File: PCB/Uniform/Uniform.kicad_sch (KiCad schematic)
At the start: 156 parts, among them CON1 826629-5, CON2 Conn_01x03, U1 STM32L072KZT6

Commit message: about to attempt rotating the MCU
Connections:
- net C0: now also U1.6 (PA0); no longer U1.11 (PA5)
- net C1: now also U1.7 (PA1); no longer U1.12 (PA6)
- net C10: now also U1.18 (PA8); no longer U1.27 (PB4)
- net C11: now also U1.19 (PA9); no longer U1.28 (PB5)
- net C12: now also U1.20 (PA10); no longer U1.29 (PB6)
- net C13: now also U1.25 (PA15); no longer U1.30 (PB7)
- net C2: now also U1.8 (PA2); no longer U1.13 (PA7)
- net C3: now also U1.9 (PA3); no longer U1.14 (PB0)
- net C4: now also U1.10 (PA4); no longer U1.15 (PB1)
- net C5: now also U1.11 (PA5); no longer U1.18 (PA8)
- net C6: now also U1.12 (PA6); no longer U1.19 (PA9)
- net C7: now also U1.13 (PA7); no longer U1.20 (PA10)
- net C8: now also U1.14 (PB0); no longer U1.25 (PA15)
- net C9: now also U1.15 (PB1); no longer U1.26 (PB3)
- net R0: now also U1.30 (PB7); no longer U1.6 (PA0)
- net R1: now also U1.29 (PB6); no longer U1.7 (PA1)
- net R2: now also U1.28 (PB5); no longer U1.8 (PA2)
- net R3: now also U1.27 (PB4); no longer U1.9 (PA3)
- net R4: now also U1.26 (PB3); no longer U1.10 (PA4)
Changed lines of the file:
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@@
     )
   )
-  (global_label "C0" (shape input) (at 349.25 92.71 270) (fields_autoplaced)
-    (effects (font (size 1.27 1.27)) (justify right))
-    (property "Intersheet References" "${INTERSHEET_REFS}" (id 0) (at 0 0 0)
-      (effects (font (size 1.27 1.27)) hide)
-    )
-  )
-  (global_label "C9" (shape input) (at 359.41 34.29 90) (fields_autoplaced)
-    (effects (font (size 1.27 1.27)) (justify left))
-    (property "Intersheet References" "${INTERSHEET_REFS}" (id 0) (at 0 0 0)
+  (global_label "C0" (shape input) (at 323.85 67.31 180) (fields_autoplaced)
+    (effects (font (size 1.27 1.27)) (justify right))
+    (property "Intersheet References" "${INTERSHEET_REFS}" (id 0) (at 416.56 -281.94 0)
+      (effects (font (size 1.27 1.27)) hide)
+    )
+  )
+  (global_label "C9" (shape input) (at 359.41 92.71 270) (fields_autoplaced)
+    (effects (font (size 1.27 1.27)) (justify right))
+    (property "Intersheet References" "${INTERSHEET_REFS}" (id 0) (at 718.82 127 0)
       (effects (font (size 1.27 1.27)) hide)
     )
@@
     )
   )
-  (global_label "R1" (shape input) (at 323.85 69.85 180) (fields_autoplaced)
-    (effects (font (size 1.27 1.27)) (justify right))
-    (property "Intersheet References" "${INTERSHEET_REFS}" (id 0) (at 0 0 0)
+  (global_label "R1" (shape input) (at 351.79 34.29 90) (fields_autoplaced)
+    (effects (font (size 1.27 1.27)) (justify left))
+    (property "Intersheet References" "${INTERSHEET_REFS}" (id 0) (at 421.64 -289.56 0)
       (effects (font (size 1.27 1.27)) hide)
     )
@@
     )
   )
-  (global_label "R2" (shape input) (at 323.85 72.39 180) (fields_autoplaced)
-    (effects (font (size 1.27 1.27)) (justify right))
-    (property "Intersheet References" "${INTERSHEET_REFS}" (id 0) (at 0 0 0)
-      (effects (font (size 1.27 1.27)) hide)
-    )
-  )
-  (global_label "C7" (shape input) (at 382.27 64.77 0) (fields_autoplaced)
-    (effects (font (size 1.27 1.27)) (justify left))
-    (property "Intersheet References" "${INTERSHEET_REFS}" (id 0) (at 0 0 0)
+  (global_label "R2" (shape input) (at 354.33 34.29 90) (fields_autoplaced)
+    (effects (font (size 1.27 1.27)) (justify left))
+    (property "Intersheet References" "${INTERSHEET_REFS}" (id 0) (at 426.72 -289.56 0)
+      (effects (font (size 1.27 1.27)) hide)
+    )
+  )
+  (global_label "C7" (shape input) (at 354.33 92.71 270) (fields_autoplaced)
+    (effects (font (size 1.27 1.27)) (justify right))
+    (property "Intersheet References" "${INTERSHEET_REFS}" (id 0) (at 419.1 -289.56 0)
       (effects (font (size 1.27 1.27)) hide)
     )
@@
     )
   )
-  (global_label "R0" (shape input) (at 323.85 67.31 180) (fields_autoplaced)
-    (effects (font (size 1.27 1.27)) (justify right))
-    (property "Intersheet References" "${INTERSHEET_REFS}" (id 0) (at 0 0 0)
-      (effects (font (size 1.27 1.27)) hide)
-    )
-  )
-  (global_label "C3" (shape input) (at 356.87 92.71 270) (fields_autoplaced)
-    (effects (font (size 1.27 1.27)) (justify right))
-    (property "Intersheet References" "${INTERSHEET_REFS}" (id 0) (at 0 0 0)
+  (global_label "R0" (shape input) (at 349.25 34.29 90) (fields_autoplaced)
+    (effects (font (size 1.27 1.27)) (justify left))
+    (property "Intersheet References" "${INTERSHEET_REFS}" (id 0) (at 416.56 -289.56 0)
+      (effects (font (size 1.27 1.27)) hide)
+    )
+  )
+  (global_label "C3" (shape input) (at 344.17 92.71 270) (fields_autoplaced)
+    (effects (font (size 1.27 1.27)) (justify right))
+    (property "Intersheet References" "${INTERSHEET_REFS}" (id 0) (at -12.7 0 0)
       (effects (font (size 1.27 1.27)) hide)
     )
@@
     )
   )
-  (global_label "C5" (shape input) (at 382.27 69.85 0) (fields_autoplaced)
-    (effects (font (size 1.27 1.27)) (justify left))
-    (property "Intersheet References" "${INTERSHEET_REFS}" (id 0) (at 0 0 0)
+  (global_label "C5" (shape input) (at 349.25 92.71 270) (fields_autoplaced)
+    (effects (font (size 1.27 1.27)) (justify right))
+    (property "Intersheet References" "${INTERSHEET_REFS}" (id 0) (at 419.1 -289.56 0)
       (effects (font (size 1.27 1.27)) hide)
     )
@@
     )
   )
-  (global_label "R3" (shape input) (at 344.17 92.71 270) (fields_autoplaced)
-    (effects (font (size 1.27 1.27)) (justify right))
-    (property "Intersheet References" "${INTERSHEET_REFS}" (id 0) (at 0 0 0)
-      (effects (font (size 1.27 1.27)) hide)
-    )
-  )
-  (global_label "C4" (shape input) (at 359.41 92.71 270) (fields_autoplaced)
-    (effects (font (size 1.27 1.27)) (justify right))
-    (property "Intersheet References" "${INTERSHEET_REFS}" (id 0) (at 0 0 0)
+  (global_label "R3" (shape input) (at 356.87 34.29 90) (fields_autoplaced)
+    (effects (font (size 1.27 1.27)) (justify left))
+    (property "Intersheet References" "${INTERSHEET_REFS}" (id 0) (at 701.04 127 0)
+      (effects (font (size 1.27 1.27)) hide)
+    )
+  )
+  (global_label "C4" (shape input) (at 346.71 92.71 270) (fields_autoplaced)
+    (effects (font (size 1.27 1.27)) (justify right))
+    (property "Intersheet References" "${INTERSHEET_REFS}" (id 0) (at -12.7 0 0)
       (effects (font (size 1.27 1.27)) hide)
     )
@@
     )
   )
-  (global_label "R4" (shape input) (at 346.71 92.71 270) (fields_autoplaced)
-    (effects (font (size 1.27 1.27)) (justify right))
-    (property "Intersheet References" "${INTERSHEET_REFS}" (id 0) (at 0 0 0)
+  (global_label "R4" (shape input) (at 359.41 34.29 90) (fields_autoplaced)
+    (effects (font (size 1.27 1.27)) (justify left))
+    (property "Intersheet References" "${INTERSHEET_REFS}" (id 0) (at 706.12 127 0)
       (effects (font (size 1.27 1.27)) hide)
     )
@@
     )
   )
-  (global_label "C13" (shape input) (at 349.25 34.29 90) (fields_autoplaced)
-    (effects (font (size 1.27 1.27)) (justify left))
-    (property "Intersheet References" "${INTERSHEET_REFS}" (id 0) (at 0 0 0)
+  (global_label "C13" (shape input) (at 361.95 34.29 90) (fields_autoplaced)
+    (effects (font (size 1.27 1.27)) (justify left))
+    (property "Intersheet References" "${INTERSHEET_REFS}" (id 0) (at 12.7 0 0)
       (effects (font (size 1.27 1.27)) hide)
     )
@@
     )
   )
-  (global_label "C11" (shape input) (at 354.33 34.29 90) (fields_autoplaced)
-    (effects (font (size 1.27 1.27)) (justify left))
-    (property "Intersheet References" "${INTERSHEET_REFS}" (id 0) (at 0 0 0)
+  (global_label "C11" (shape input) (at 382.27 67.31 0) (fields_autoplaced)
+    (effects (font (size 1.27 1.27)) (justify left))
+    (property "Intersheet References" "${INTERSHEET_REFS}" (id 0) (at 416.56 -287.02 0)
       (effects (font (size 1.27 1.27)) hide)
     )
@@
     )
   )
-  (global_label "C8" (shape input) (at 361.95 34.29 90) (fields_autoplaced)
-    (effects (font (size 1.27 1.27)) (justify left))
-    (property "Intersheet References" "${INTERSHEET_REFS}" (id 0) (at 0 0 0)
-      (effects (font (size 1.27 1.27)) hide)
-    )
-  )
-  (global_label "C6" (shape input) (at 382.27 67.31 0) (fields_autoplaced)
-    (effects (font (size 1.27 1.27)) (justify left))
-    (property "Intersheet References" "${INTERSHEET_REFS}" (id 0) (at 0 0 0)
-      (effects (font (size 1.27 1.27)) hide)
-    )
-  )
-  (global_label "C2" (shape input) (at 354.33 92.71 270) (fields_autoplaced)
-    (effects (font (size 1.27 1.27)) (justify right))
-    (property "Intersheet References" "${INTERSHEET_REFS}" (id 0) (at 0 0 0)
+  (global_label "C8" (shape input) (at 356.87 92.71 270) (fields_autoplaced)
+    (effects (font (size 1.27 1.27)) (justify right))
+    (property "Intersheet References" "${INTERSHEET_REFS}" (id 0) (at 718.82 127 0)
+      (effects (font (size 1.27 1.27)) hide)
+    )
+  )
+  (global_label "C6" (shape input) (at 351.79 92.71 270) (fields_autoplaced)
+    (effects (font (size 1.27 1.27)) (justify right))
+    (property "Intersheet References" "${INTERSHEET_REFS}" (id 0) (at 419.1 -289.56 0)
+      (effects (font (size 1.27 1.27)) hide)
+    )
+  )
+  (global_label "C2" (shape input) (at 323.85 72.39 180) (fields_autoplaced)
+    (effects (font (size 1.27 1.27)) (justify right))
+    (property "Intersheet References" "${INTERSHEET_REFS}" (id 0) (at 416.56 -281.94 0)
       (effects (font (size 1.27 1.27)) hide)
     )
@@
     )
   )
-  (global_label "C1" (shape input) (at 351.79 92.71 270) (fields_autoplaced)
-    (effects (font (size 1.27 1.27)) (justify right))
-    (property "Intersheet References" "${INTERSHEET_REFS}" (id 0) (at 0 0 0)
-      (effects (font (size 1.27 1.27)) hide)
-    )
-  )
-  (global_label "C10" (shape input) (at 356.87 34.29 90) (fields_autoplaced)
-    (effects (font (size 1.27 1.27)) (justify left))
-    (property "Intersheet References" "${INTERSHEET_REFS}" (id 0) (at 0 0 0)
+  (global_label "C1" (shape input) (at 323.85 69.85 180) (fields_autoplaced)
+    (effects (font (size 1.27 1.27)) (justify right))
+    (property "Intersheet References" "${INTERSHEET_REFS}" (id 0) (at 416.56 -281.94 0)
+      (effects (font (size 1.27 1.27)) hide)
+    )
+  )
+  (global_label "C10" (shape input) (at 382.27 69.85 0) (fields_autoplaced)
+    (effects (font (size 1.27 1.27)) (justify left))
+    (property "Intersheet References" "${INTERSHEET_REFS}" (id 0) (at 416.56 -287.02 0)
       (effects (font (size 1.27 1.27)) hide)
     )
@@
     )
   )
-  (global_label "C12" (shape input) (at 351.79 34.29 90) (fields_autoplaced)
-    (effects (font (size 1.27 1.27)) (justify left))
-    (property "Intersheet References" "${INTERSHEET_REFS}" (id 0) (at 0 0 0)
-      (effects (font (size 1.27 1.27)) hide)
-    )
+  (global_label "C12" (shape input) (at 382.27 64.77 0) (fields_autoplaced)
+    (effects (font (size 1.27 1.27)) (justify left))
+    (property "Intersheet References" "${INTERSHEET_REFS}" (id 0) (at 416.56 -287.02 0)
+      (effects (font (size 1.27 1.27)) hide)
+    )

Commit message: PCB first pass complete
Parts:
- LED1: footprint LED_THT:LED_D5.0mm_Clear -> LED_THT:LED_D3.0mm_Clear
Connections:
- net C13: now also U1.29 (PB6); no longer U1.25 (PA15)
- net LED_DATA: now also U1.26 (PB3); no longer U1.2 (PC14-_OSC32_IN_(PC14))
- net R0: now also U1.27 (PB4); no longer U1.30 (PB7)
- net R1: now also U1.28 (PB5); no longer U1.29 (PB6)
- net R2: now also U1.30 (PB7); no longer U1.28 (PB5)
- net R3: now also U1.3 (PC15-_OSC32_OUT_(PC15)); no longer U1.27 (PB4)
- net R4: now also U1.2 (PC14-_OSC32_IN_(PC14)); no longer U1.26 (PB3)
- net STATUS_LED_DATA: now also U1.25 (PA15); no longer U1.3 (PC15-_OSC32_OUT_(PC15))
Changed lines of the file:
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@@
     )
   )
-  (global_label "R1" (shape input) (at 351.79 34.29 90) (fields_autoplaced)
+  (global_label "R1" (shape input) (at 354.33 34.29 90) (fields_autoplaced)
     (effects (font (size 1.27 1.27)) (justify left))
-    (property "Intersheet References" "${INTERSHEET_REFS}" (id 0) (at 421.64 -289.56 0)
+    (property "Intersheet References" "${INTERSHEET_REFS}" (id 0) (at 424.18 -289.56 0)
       (effects (font (size 1.27 1.27)) hide)
     )
@@
     )
   )
-  (global_label "STATUS_LED_DATA" (shape input) (at 323.85 59.69 180) (fields_autoplaced)
-    (effects (font (size 1.27 1.27)) (justify right))
-    (property "Intersheet References" "${INTERSHEET_REFS}" (id 0) (at 0 0 0)
+  (global_label "STATUS_LED_DATA" (shape input) (at 361.95 34.29 90) (fields_autoplaced)
+    (effects (font (size 1.27 1.27)) (justify left))
+    (property "Intersheet References" "${INTERSHEET_REFS}" (id 0) (at 421.64 -289.56 0)
       (effects (font (size 1.27 1.27)) hide)
     )
@@
     )
   )
-  (global_label "R2" (shape input) (at 354.33 34.29 90) (fields_autoplaced)
+  (global_label "R2" (shape input) (at 349.25 34.29 90) (fields_autoplaced)
     (effects (font (size 1.27 1.27)) (justify left))
-    (property "Intersheet References" "${INTERSHEET_REFS}" (id 0) (at 426.72 -289.56 0)
+    (property "Intersheet References" "${INTERSHEET_REFS}" (id 0) (at 421.64 -289.56 0)
       (effects (font (size 1.27 1.27)) hide)
     )
@@
     )
   )
-  (global_label "R0" (shape input) (at 349.25 34.29 90) (fields_autoplaced)
+  (global_label "R0" (shape input) (at 356.87 34.29 90) (fields_autoplaced)
     (effects (font (size 1.27 1.27)) (justify left))
-    (property "Intersheet References" "${INTERSHEET_REFS}" (id 0) (at 416.56 -289.56 0)
+    (property "Intersheet References" "${INTERSHEET_REFS}" (id 0) (at 424.18 -289.56 0)
       (effects (font (size 1.27 1.27)) hide)
     )
@@
     )
   )
-  (global_label "R3" (shape input) (at 356.87 34.29 90) (fields_autoplaced)
-    (effects (font (size 1.27 1.27)) (justify left))
-    (property "Intersheet References" "${INTERSHEET_REFS}" (id 0) (at 701.04 127 0)
+  (global_label "R3" (shape input) (at 323.85 59.69 180) (fields_autoplaced)
+    (effects (font (size 1.27 1.27)) (justify right))
+    (property "Intersheet References" "${INTERSHEET_REFS}" (id 0) (at 416.56 -284.48 0)
       (effects (font (size 1.27 1.27)) hide)
     )
@@
     )
   )
-  (global_label "R4" (shape input) (at 359.41 34.29 90) (fields_autoplaced)
-    (effects (font (size 1.27 1.27)) (justify left))
-    (property "Intersheet References" "${INTERSHEET_REFS}" (id 0) (at 706.12 127 0)
+  (global_label "R4" (shape input) (at 323.85 57.15 180) (fields_autoplaced)
+    (effects (font (size 1.27 1.27)) (justify right))
+    (property "Intersheet References" "${INTERSHEET_REFS}" (id 0) (at 416.56 -289.56 0)
       (effects (font (size 1.27 1.27)) hide)
     )
@@
     )
   )
-  (global_label "C13" (shape input) (at 361.95 34.29 90) (fields_autoplaced)
+  (global_label "C13" (shape input) (at 351.79 34.29 90) (fields_autoplaced)
     (effects (font (size 1.27 1.27)) (justify left))
-    (property "Intersheet References" "${INTERSHEET_REFS}" (id 0) (at 12.7 0 0)
+    (property "Intersheet References" "${INTERSHEET_REFS}" (id 0) (at 2.54 0 0)
       (effects (font (size 1.27 1.27)) hide)
     )
@@
     )
   )
-  (global_label "LED_DATA" (shape input) (at 323.85 57.15 180) (fields_autoplaced)
-    (effects (font (size 1.27 1.27)) (justify right))
-    (property "Intersheet References" "${INTERSHEET_REFS}" (id 0) (at 0 0 0)
+  (global_label "LED_DATA" (shape input) (at 359.41 34.29 90) (fields_autoplaced)
+    (effects (font (size 1.27 1.27)) (justify left))
+    (property "Intersheet References" "${INTERSHEET_REFS}" (id 0) (at 416.56 -289.56 0)
       (effects (font (size 1.27 1.27)) hide)
     )
@@
     (property "Reference" "LED1" (id 0) (at 272.8722 22.4282 0))
     (property "Value" "LED" (id 1) (at 272.8722 24.7396 0))
-    (property "Footprint" "LED_THT:LED_D5.0mm_Clear" (id 2) (at 273.05 27.94 0)
+    (property "Footprint" "LED_THT:LED_D3.0mm_Clear" (id 2) (at 273.05 27.94 0)
       (effects (font (size 1.27 1.27)) hide)
     )
@@
     )
     (path "/00000000-0000-0000-0000-0000646a674a"
-      (reference "LED1") (unit 1) (value "LED") (footprint "LED_THT:LED_D5.0mm_Clear")
+      (reference "LED1") (unit 1) (value "LED") (footprint "LED_THT:LED_D3.0mm_Clear")
     )
     (path "/00000000-0000-0000-0000-000063eb21f8"

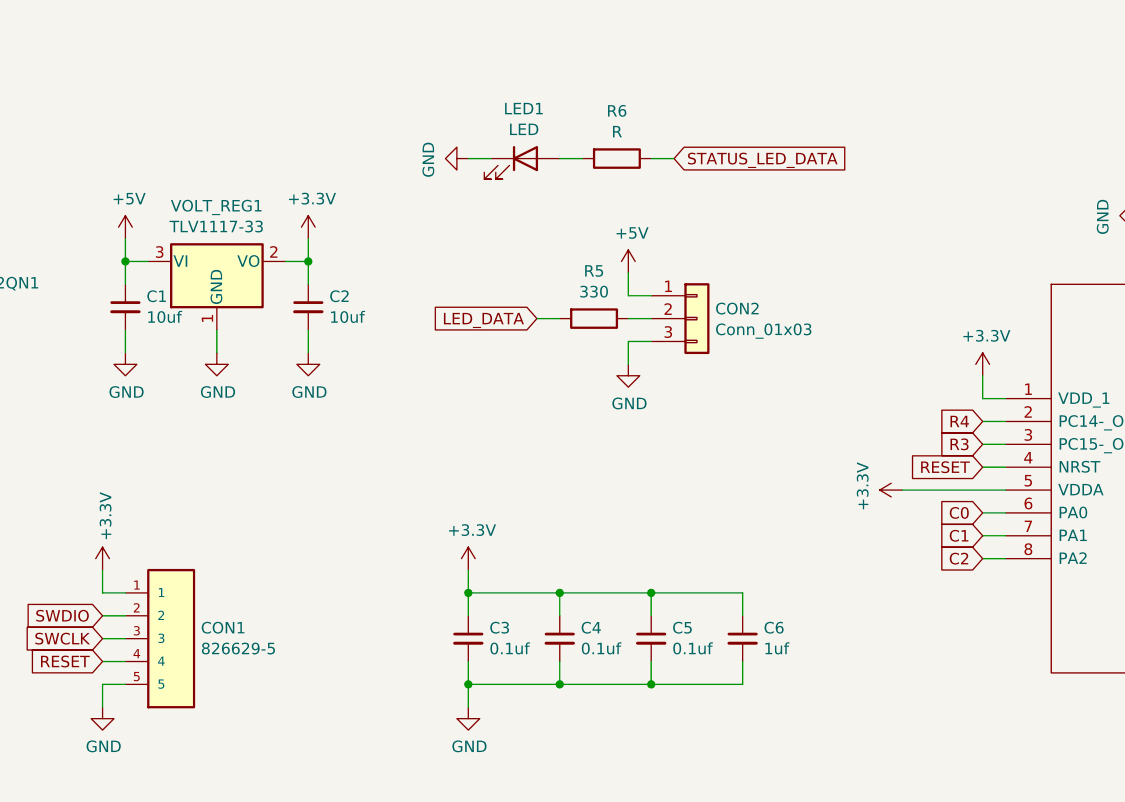
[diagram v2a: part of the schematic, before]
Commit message: Added Neopixel status LED, moved mount holes, and re-routed traces to fit new status led type
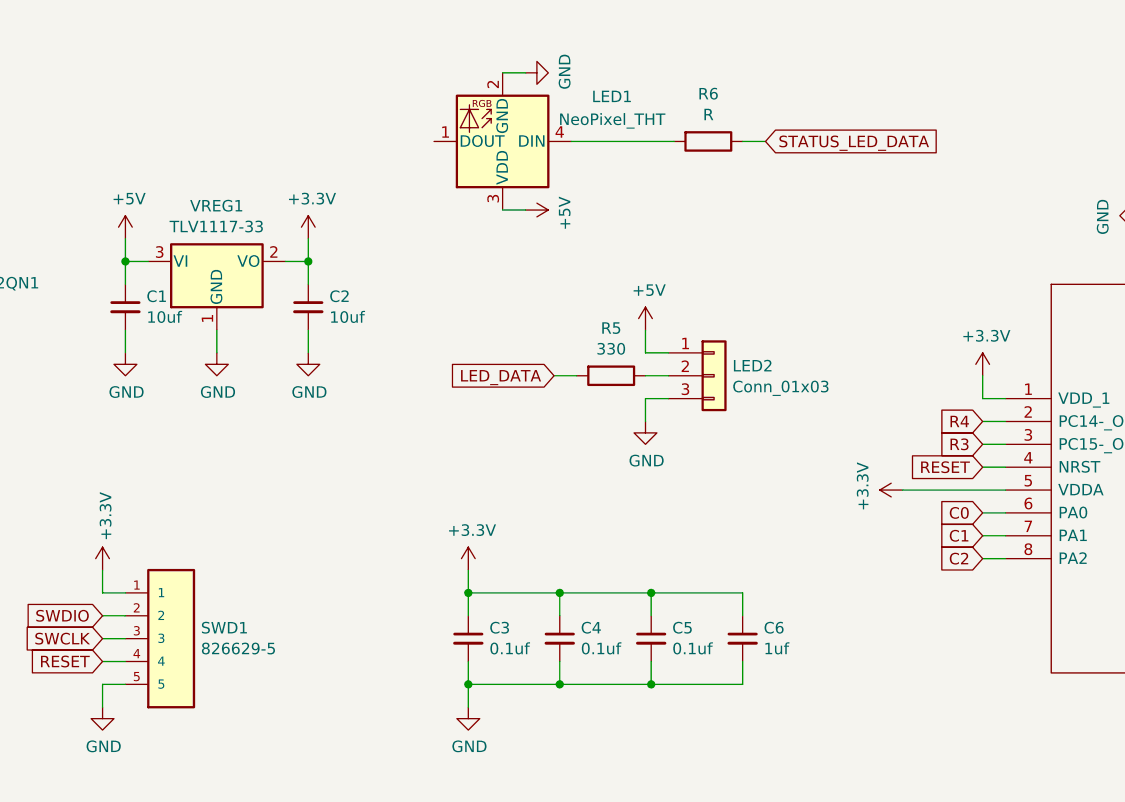
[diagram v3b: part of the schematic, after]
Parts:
- removed LED1: LED, LED_THT:LED_D3.0mm_Clear, symbol Device:LED
- added LED1: NeoPixel_THT, LED_THT:LED_D5.0mm-4_RGB, symbol LED:NeoPixel_THT
- renumbered CON2 to LED2, CON1 to SWD1, VOLT_REG1 to VREG1
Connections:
- net +5V: now also LED1.3 (VDD)
- net GND: now also LED1.2 (GND)
- net at R6.2: now also LED1.4 (DIN)
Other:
- moved on the sheet: LED2, R5, R6

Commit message: reduced neopixel pin drill hole size from .9 to .8 to accomodate typical minimum manufacturing hole spacing requirements
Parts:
- LED1: footprint LED_THT:LED_D5.0mm-4_RGB -> Neopixel:LED_D5.0mm-4_RGB
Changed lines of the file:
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@@
     (property "Reference" "LED1" (id 0) (at 282.6604 21.0778 0))
     (property "Value" "NeoPixel_THT" (id 1) (at 282.6604 23.6147 0))
-    (property "Footprint" "LED_THT:LED_D5.0mm-4_RGB" (id 2) (at 269.24 18.415 0)
+    (property "Footprint" "Neopixel:LED_D5.0mm-4_RGB" (id 2) (at 269.24 18.415 0)
       (effects (font (size 1.27 1.27)) (justify left top) hide)
     )
@@
     )
     (path "/cf57663d-643d-451e-b65d-af3e28d7b99a"
-      (reference "LED1") (unit 1) (value "NeoPixel_THT") (footprint "LED_THT:LED_D5.0mm-4_RGB")
+      (reference "LED1") (unit 1) (value "NeoPixel_THT") (footprint "Neopixel:LED_D5.0mm-4_RGB")
     )
     (path "/00000000-0000-0000-0000-00006398fb89"
